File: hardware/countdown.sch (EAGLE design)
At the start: 30 parts, among them J1 BURNIN, J2 USB, J3 LiPo, J4 OLED, J5 TOP, J6 BASE, U1 DS3231MZ+TRL_SOIC8, U2 ATMEGA328P-AUR, U3 MCP73831T, U4 BL1551

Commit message: prepare for order
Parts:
- R2: value 125k -> 51k
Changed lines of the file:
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@@
 <part name="C7" library="scono" library_urn="urn:adsk.eagle:library:14850048" deviceset="CAP" device="0402-CAP" package3d_urn="urn:adsk.eagle:package:14850678/3" value="1uF"/>
 <part name="U$1" library="scono" library_urn="urn:adsk.eagle:library:14850048" deviceset="CL-SB-12C-12" device=""/>
-<part name="R2" library="scono" library_urn="urn:adsk.eagle:library:14850048" deviceset="R-US_" device="R0402" package3d_urn="urn:adsk.eagle:package:14850590/3" value="125k"/>
+<part name="R2" library="scono" library_urn="urn:adsk.eagle:library:14850048" deviceset="R-US_" device="R0402" package3d_urn="urn:adsk.eagle:package:14850590/3" value="51k"/>
 <part name="J4" library="scono" library_urn="urn:adsk.eagle:library:14850048" deviceset="CONN_04" device="1X04_NO_SILK" package3d_urn="urn:adsk.eagle:package:38094/1" value="OLED"/>
 <part name="R3" library="scono" library_urn="urn:adsk.eagle:library:14850048" deviceset="R-US_" device="R0402" package3d_urn="urn:adsk.eagle:package:14850590/3" value="1k"/>

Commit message: jlc order done
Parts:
- added C8: 0.1uF, scono:CAP0402-CAP
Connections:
- net GND_TOP: now also C8.1
- net INT_WAKE: now also C8.2
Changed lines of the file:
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@@
 <part name="D2" library="scono" library_urn="urn:adsk.eagle:library:14850048" deviceset="LED" device="0603" package3d_urn="urn:adsk.eagle:package:14850721/3"/>
 <part name="R7" library="scono" library_urn="urn:adsk.eagle:library:14850048" deviceset="R-US_" device="R0402" package3d_urn="urn:adsk.eagle:package:14850590/3" value="330R"/>
+<part name="C8" library="scono" library_urn="urn:adsk.eagle:library:14850048" deviceset="CAP" device="0402-CAP" package3d_urn="urn:adsk.eagle:package:14850678/3" value="0.1uF"/>
 </parts>
 <sheets>
@@
 <attribute name="VALUE" x="85.09" y="7.62" size="1.016" layer="96" rot="R90" align="top-left"/>
 </instance>
+<instance part="C8" gate="G$1" x="233.68" y="116.84" smashed="yes" rot="R90">
+<attribute name="NAME" x="232.156" y="115.57" size="1.016" layer="95" rot="R90"/>
+<attribute name="VALUE" x="236.22" y="115.57" size="1.016" layer="96" rot="R90"/>
+</instance>
 </instances>
 <busses>
@@
 <wire x1="220.98" y1="109.22" x2="220.98" y2="111.76" width="0.1524" layer="91"/>
 <label x="220.98" y="109.22" size="1.778" layer="95"/>
+<pinref part="C8" gate="G$1" pin="1"/>
+<wire x1="233.68" y1="114.3" x2="233.68" y2="109.22" width="0.1524" layer="91"/>
+<wire x1="233.68" y1="109.22" x2="220.98" y2="109.22" width="0.1524" layer="91"/>
 </segment>
 </net>
@@
 <pinref part="R6" gate="G$1" pin="2"/>
 <label x="220.98" y="121.92" size="1.778" layer="95"/>
-</segment>
-<segment>
+<pinref part="C8" gate="G$1" pin="2"/>
+<wire x1="220.98" y1="119.38" x2="233.68" y2="119.38" width="0.1524" layer="91"/>
+<junction x="220.98" y="119.38"/>
+</segment>
+<segment>

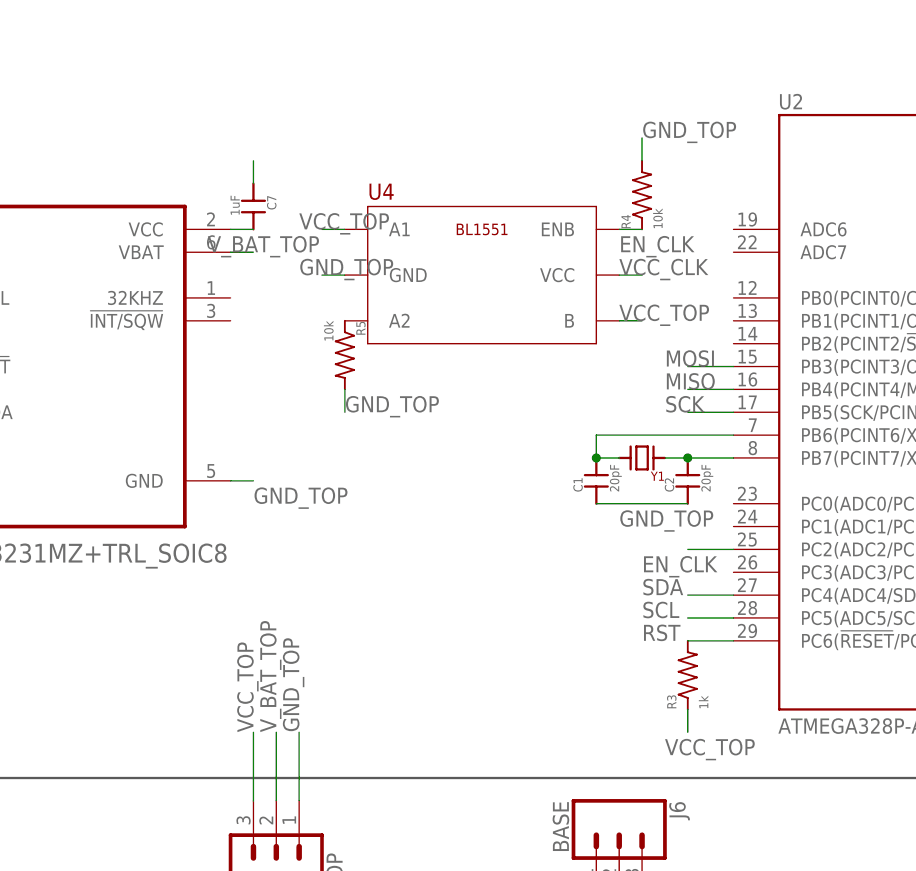
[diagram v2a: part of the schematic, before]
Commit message: small fixes to board from debugging
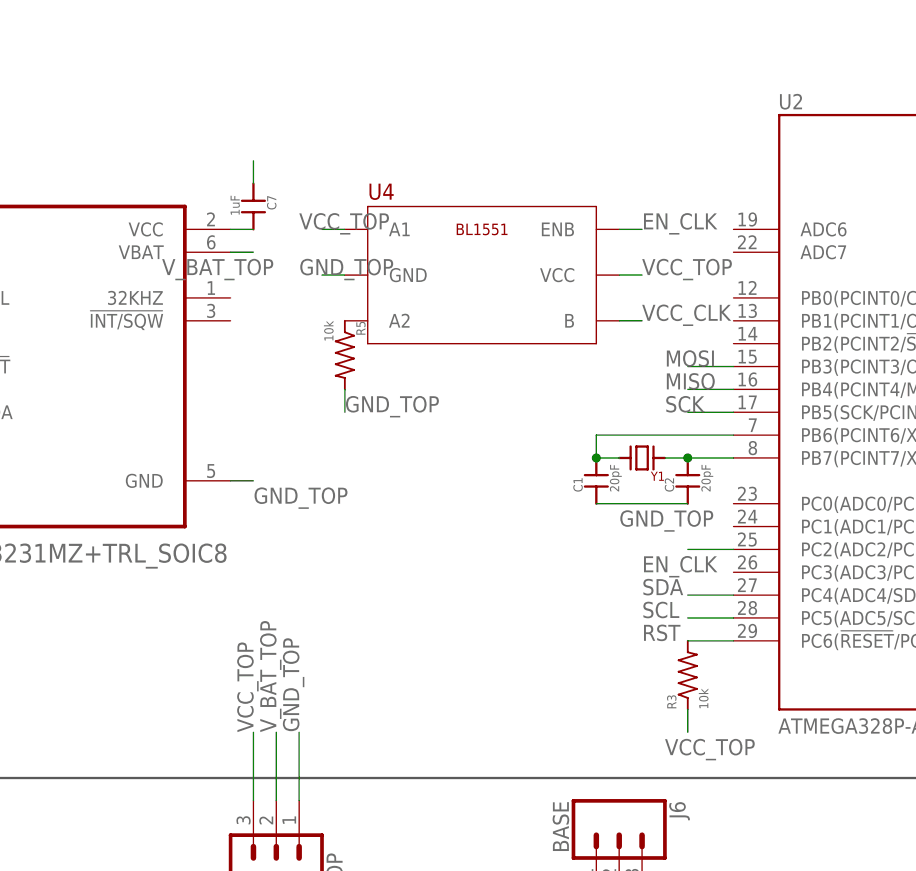
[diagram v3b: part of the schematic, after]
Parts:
- removed R4: 10k, scono:R-US_R0402
- R3: value 1k -> 10k
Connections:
- net EN_CLK: no longer R4.1
- net GND_TOP: no longer R4.2
- net VCC_CLK: now also U4.B; no longer U4.VCC
- net VCC_TOP: now also U4.VCC; no longer U4.B
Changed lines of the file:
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@@
 <part name="R2" library="scono" library_urn="urn:adsk.eagle:library:14850048" deviceset="R-US_" device="R0402" package3d_urn="urn:adsk.eagle:package:14850590/3" value="51k"/>
 <part name="J4" library="scono" library_urn="urn:adsk.eagle:library:14850048" deviceset="CONN_04" device="1X04_NO_SILK" package3d_urn="urn:adsk.eagle:package:38094/1" value="OLED"/>
-<part name="R3" library="scono" library_urn="urn:adsk.eagle:library:14850048" deviceset="R-US_" device="R0402" package3d_urn="urn:adsk.eagle:package:14850590/3" value="1k"/>
+<part name="R3" library="scono" library_urn="urn:adsk.eagle:library:14850048" deviceset="R-US_" device="R0402" package3d_urn="urn:adsk.eagle:package:14850590/3" value="10k"/>
 <part name="BT1" library="scono" library_urn="urn:adsk.eagle:library:14850048" deviceset="BK-916-TR" device=""/>
 <part name="U4" library="scono" library_urn="urn:adsk.eagle:library:14850048" deviceset="BL1551" device=""/>
-<part name="R4" library="scono" library_urn="urn:adsk.eagle:library:14850048" deviceset="R-US_" device="R0402" package3d_urn="urn:adsk.eagle:package:14850590/3" value="10k"/>
 <part name="R5" library="scono" library_urn="urn:adsk.eagle:library:14850048" deviceset="R-US_" device="R0402" package3d_urn="urn:adsk.eagle:package:14850590/3" value="10k"/>
 <part name="J5" library="scono" library_urn="urn:adsk.eagle:library:14850048" deviceset="CONN_03" device="1X03_NO_SILK" package3d_urn="urn:adsk.eagle:package:38076/1" value="TOP"/>
@@
 <attribute name="NAME" x="81.28" y="165.1" size="1.778" layer="94" align="top-left"/>
 </instance>
-<instance part="R4" gate="G$1" x="111.76" y="165.1" smashed="yes" rot="R90">
-<attribute name="NAME" x="110.49" y="160.02" size="1.016" layer="95" rot="R90"/>
-<attribute name="VALUE" x="113.03" y="160.02" size="1.016" layer="96" rot="R90" align="top-left"/>
-</instance>
 <instance part="R5" gate="G$1" x="78.74" y="144.78" smashed="yes" rot="R270">
 <attribute name="NAME" x="80.01" y="149.86" size="1.016" layer="95" rot="R270"/>
@@
 </segment>
 <segment>
-<pinref part="U4" gate="A" pin="VCC"/>
-<wire x1="111.76" y1="154.94" x2="109.22" y2="154.94" width="0.1524" layer="91"/>
-<label x="109.22" y="154.94" size="1.778" layer="95"/>
+<pinref part="U4" gate="A" pin="B"/>
+<wire x1="111.76" y1="149.86" x2="109.22" y2="149.86" width="0.1524" layer="91"/>
+<label x="111.76" y="149.86" size="1.778" layer="95"/>
 </segment>
 </net>
@@
 <pinref part="U4" gate="A" pin="ENB"/>
 <wire x1="111.76" y1="160.02" x2="109.22" y2="160.02" width="0.1524" layer="91"/>
-<label x="109.22" y="157.48" size="1.778" layer="95"/>
-<pinref part="R4" gate="G$1" pin="1"/>
+<label x="111.76" y="160.02" size="1.778" layer="95"/>
 </segment>
 <segment>
@@
 <wire x1="76.2" y1="154.94" x2="78.74" y2="154.94" width="0.1524" layer="91"/>
 <label x="73.66" y="154.94" size="1.778" layer="95"/>
-</segment>
-<segment>
-<pinref part="R4" gate="G$1" pin="2"/>
-<wire x1="111.76" y1="170.18" x2="111.76" y2="167.64" width="0.1524" layer="91"/>
-<label x="111.76" y="170.18" size="1.778" layer="95"/>
 </segment>
 <segment>
@@
 <pinref part="U1" gate="G$1" pin="VBAT"/>
 <wire x1="68.58" y1="157.48" x2="66.04" y2="157.48" width="0.1524" layer="91"/>
-<label x="63.5" y="157.48" size="1.778" layer="95"/>
+<label x="58.42" y="154.94" size="1.778" layer="95"/>
 </segment>
 </net>
@@
 </segment>
 <segment>
-<pinref part="U4" gate="A" pin="B"/>
-<wire x1="111.76" y1="149.86" x2="109.22" y2="149.86" width="0.1524" layer="91"/>
-<label x="109.22" y="149.86" size="1.778" layer="95"/>
-</segment>
-<segment>
 <pinref part="R3" gate="G$1" pin="1"/>
 <wire x1="116.84" y1="104.14" x2="116.84" y2="106.68" width="0.1524" layer="91"/>
@@
 <label x="220.98" y="137.16" size="1.778" layer="95"/>
 </segment>
-</net>
+<segment>
+<pinref part="U4" gate="A" pin="VCC"/>
+<wire x1="111.76" y1="154.94" x2="109.22" y2="154.94" width="0.1524" layer="91"/>
+<label x="111.76" y="154.94" size="1.778" layer="95"/>
+</segment>
+</net>
